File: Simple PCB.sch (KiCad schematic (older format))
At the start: 1 part

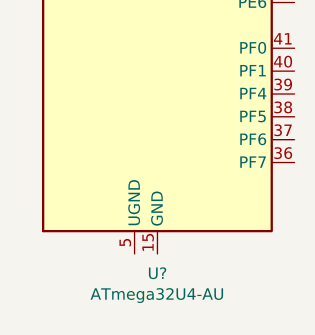
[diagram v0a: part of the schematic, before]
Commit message: Added ground
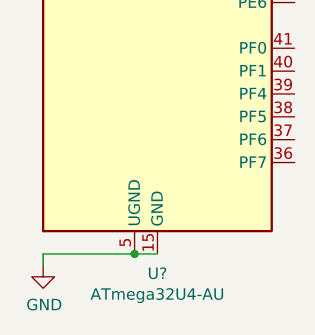
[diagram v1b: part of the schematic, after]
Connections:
- net GND: now reaches U?.15 (GND), U?.23 (GND), U?.35 (GND), U?.43 (GND)
- net GND: now also U?.5 (UGND)
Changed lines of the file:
@@
 EESchema Schematic File Version 4
+LIBS:Simple PCB-cache
 EELAYER 26 0
 EELAYER END
@@
 Wire Wire Line
 	1800 2100 1700 2100
+$Comp
+L power:GND #PWR?
+U 1 1 5C756188
+P 1300 5750
+F 0 "#PWR?" H 1300 5500 50  0001 C CNN
+F 1 "GND" H 1305 5577 50  0000 C CNN
+F 2 "" H 1300 5750 50  0001 C CNN
+F 3 "" H 1300 5750 50  0001 C CNN
+	1    1300 5750
+	1    0    0    -1
+$EndComp
+Wire Wire Line
+	1800 5700 1700 5700
+Wire Wire Line
+	1700 5700 1300 5700
+Wire Wire Line
+	1300 5700 1300 5750
+Connection ~ 1700 5700
 $EndSCHEMATC

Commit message: Finished MCU
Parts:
- added C?: 1uF, symbol Device:C_Small
- added C? (x4): 0.1uF, symbol Device:C_Small
- added C? (x2): 22pF, symbol Device:C_Small
- added R? (x2): 10k, symbol Device:R_Small
- added R? (x2): 22, symbol Device:R_Small
- added SW?: SW_Push, symbol Switch:SW_Push
- added Y?: 16MHz, symbol Device:Crystal_GND24_Small
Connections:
- net +5V: now also U?.7 (VBUS), C?.1, C?.1, C?.1, C?.1, R?.2
- net GND: now also C?.2, C?.2, C?.2, C?.2, C?.2, C?.2, C?.2, R?.1, SW?.1, Y?.2, Y?.4
- net at U?.13 (~RESET): now also R?.1, SW?.2
- net at U?.16 (XTAL2): now also C?.1, Y?.3
- net at U?.17 (XTAL1): now also C?.1, Y?.1
- net at U?.3 (D-): now also R?.1
- net at U?.33 (~HWB~/PE2): now also R?.2
- net at U?.4 (D+): now also R?.1
- net at U?.6 (UCAP): now also C?.1
- new net D+: R?.2
- new net D-: R?.2
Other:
- moved on the sheet: U?

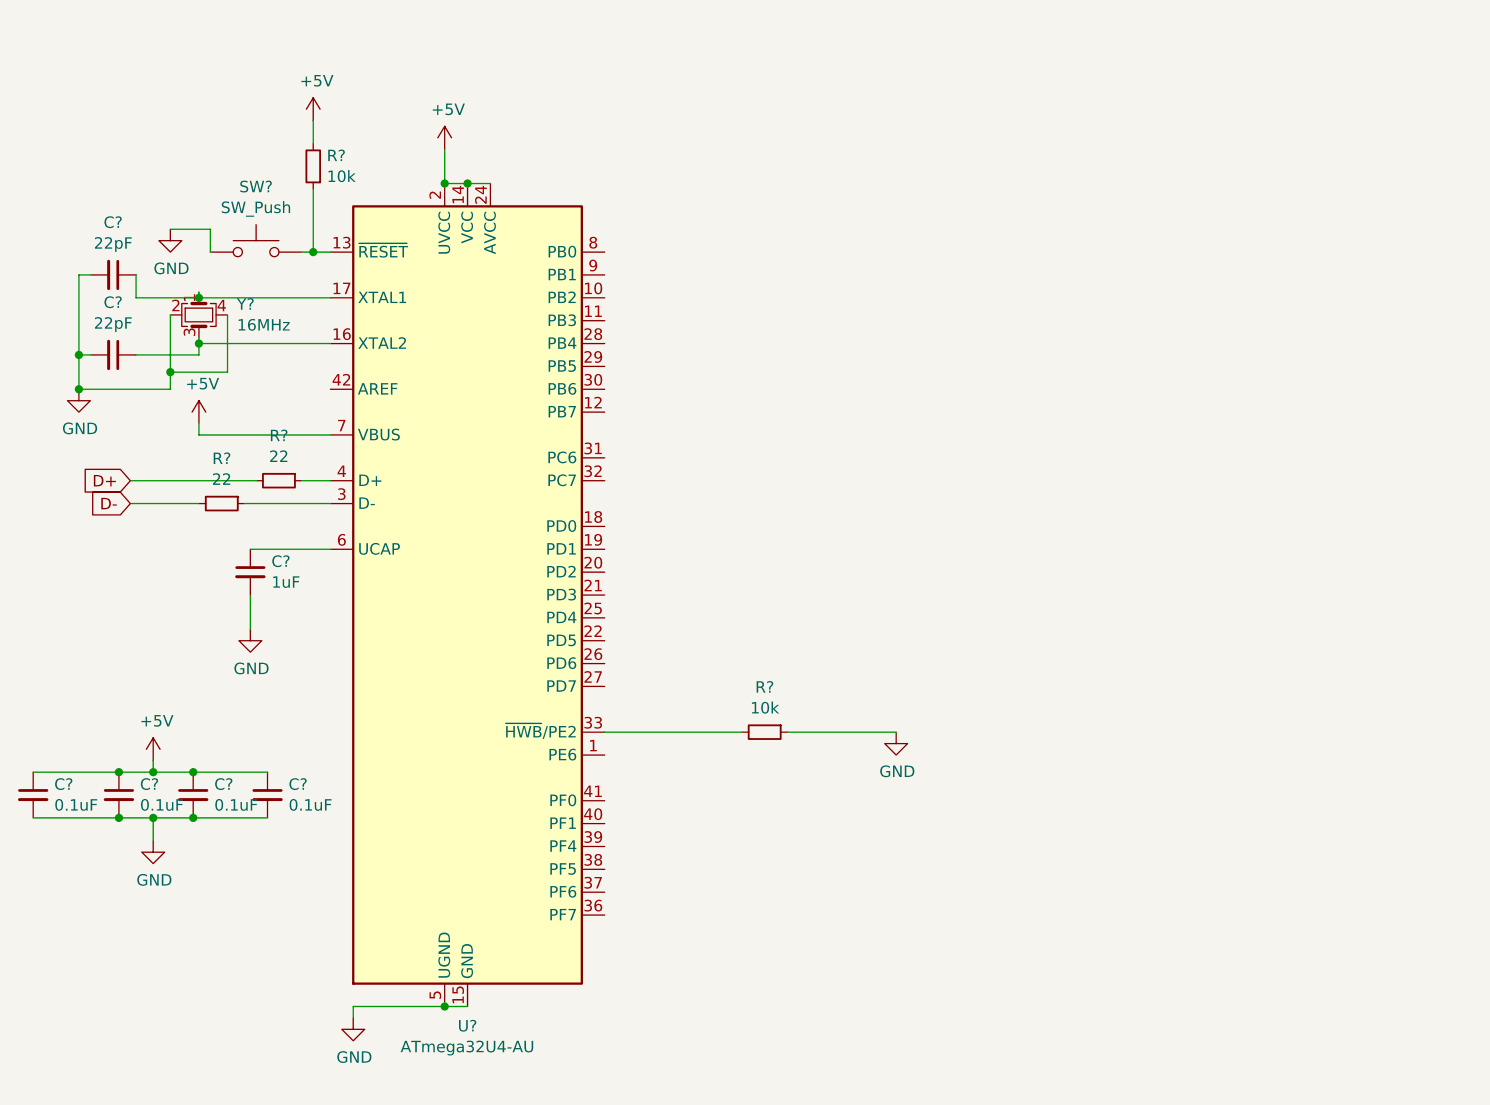
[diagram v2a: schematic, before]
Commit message: Added USB Connector and rows and collums
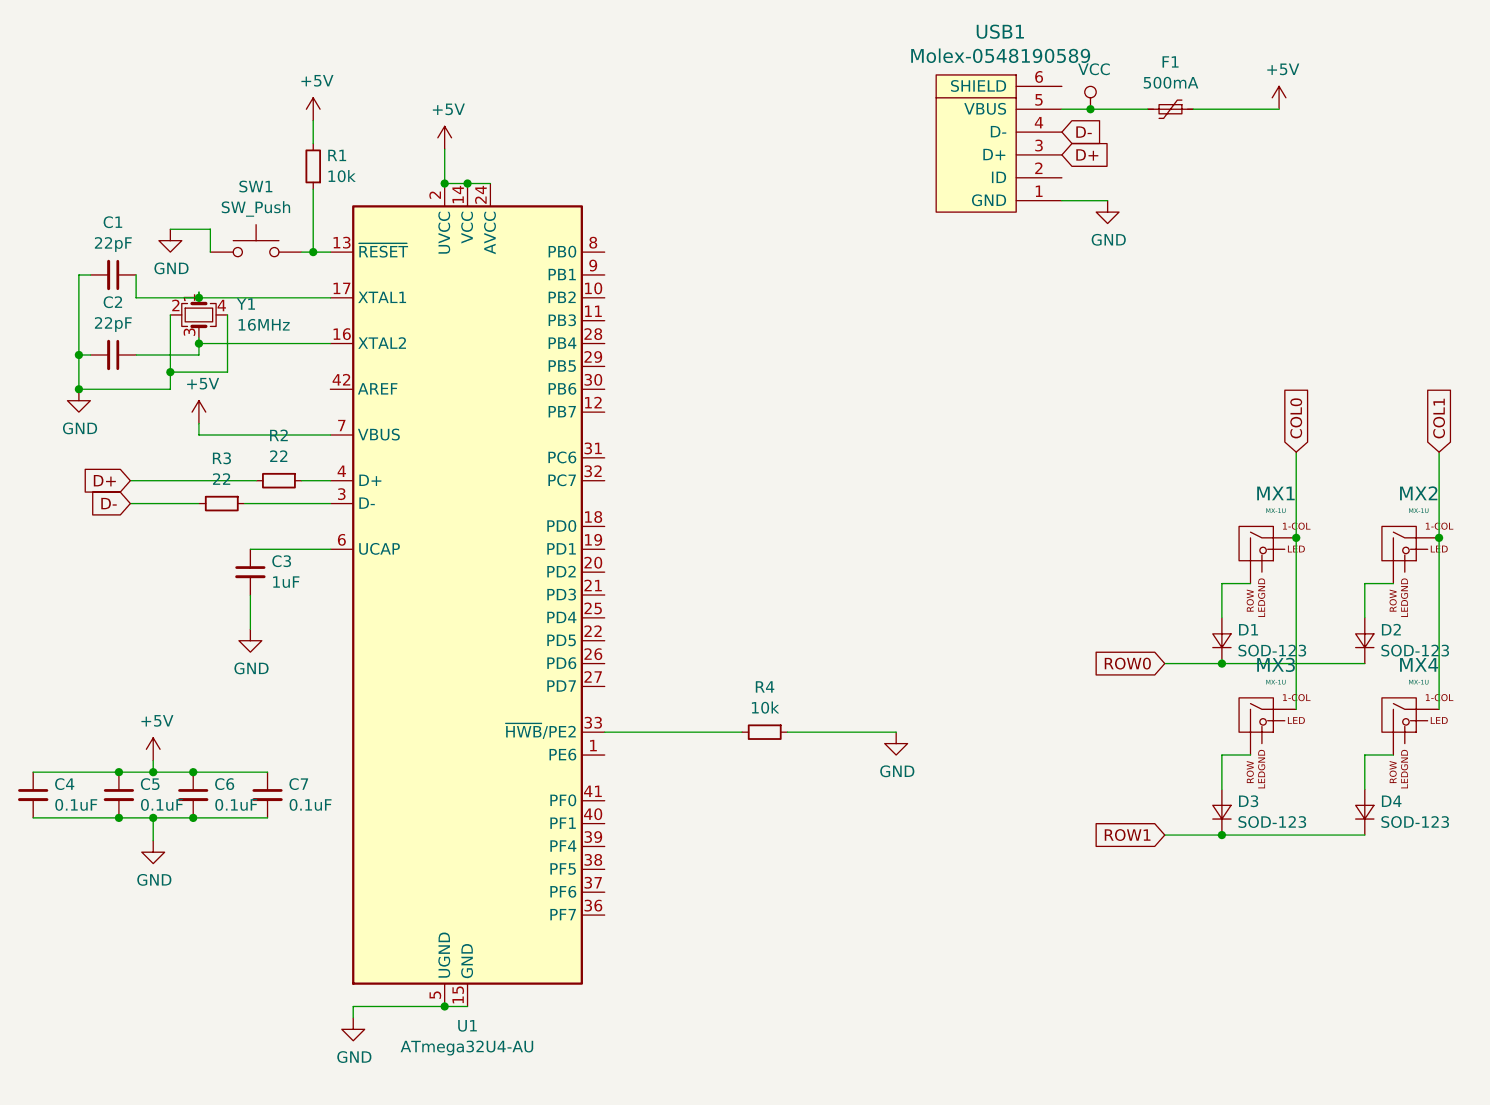
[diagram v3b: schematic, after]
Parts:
- added D1, D2, D3, D4: SOD-123, symbol Device:D_Small
- added F1: 500mA, symbol Device:Polyfuse_Small
- added MX1, MX2, MX3, MX4: MX-1U, symbol MX_Alps_Hybrids:MX-1U
- added USB1: Molex-0548190589, symbol random-keyboard-parts:Molex-0548190589
- gave numbers to parts that had none: 14
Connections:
- net +5V: now also F1.1
- net D+: now also USB1.3 (D+)
- net D-: now also USB1.4 (D-)
- net GND: now also USB1.1 (GND)
- new net: D3.2 (A), MX3.2 (ROW)
- new net: D4.2 (A), MX4.2 (ROW)
- new net: D1.2 (A), MX1.2 (ROW)
- new net: D2.2 (A), MX2.2 (ROW)
- new net COL0: MX1.1 (COL), MX3.1 (COL)
- new net COL1: MX2.1 (COL), MX4.1 (COL)
- new net ROW0: D1.1 (K), D2.1 (K)
- new net ROW1: D3.1 (K), D4.1 (K)
- new net VCC: F1.2, USB1.5 (VBUS)

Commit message: Assigned most footprints
Need to fix 32u4 mcu
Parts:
- C1, C2, C3, C4, C5, C6, C7: footprint (none) -> Capacitor_SMD:C_0805_2012Metric
- D1, D2, D3, D4: footprint (none) -> Diode_SMD:D_SOD-123
- F1: footprint (none) -> Fuse:Fuse_1206_3216Metric
- MX1, MX2, MX3, MX4: footprint (none) -> MX_Alps_Hybrid:MX-1U
- R1, R2, R3, R4: footprint (none) -> Resistor_SMD:R_0805_2012Metric
- SW1: footprint (none) -> random-keyboard-parts:SKQG-1155865
- USB1: footprint (none) -> random-keyboard-parts:Molex-0548190589
- Y1: footprint (none) -> Crystal:Crystal_SMD_3225-4Pin_3.2x2.5mm
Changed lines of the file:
@@
 F 0 "R4" V 4204 4425 50  0000 C CNN
 F 1 "10k" V 4295 4425 50  0000 C CNN
-F 2 "" H 4400 4425 50  0001 C CNN
+F 2 "Resistor_SMD:R_0805_2012Metric" H 4400 4425 50  0001 C CNN
 F 3 "~" H 4400 4425 50  0001 C CNN
 	1    4400 4425
@@
 F 0 "R2" V 2079 3325 50  0000 C CNN
 F 1 "22" V 2170 3325 50  0000 C CNN
-F 2 "" H 2275 3325 50  0001 C CNN
+F 2 "Resistor_SMD:R_0805_2012Metric" H 2275 3325 50  0001 C CNN
 F 3 "~" H 2275 3325 50  0001 C CNN
 	1    2275 3325
@@
 F 0 "R3" V 1829 3425 50  0000 C CNN
 F 1 "22" V 1920 3425 50  0000 C CNN
-F 2 "" H 2025 3425 50  0001 C CNN
+F 2 "Resistor_SMD:R_0805_2012Metric" H 2025 3425 50  0001 C CNN
 F 3 "~" H 2025 3425 50  0001 C CNN
 	1    2025 3425
@@
 F 0 "C3" H 2242 3771 50  0000 L CNN
 F 1 "1uF" H 2242 3680 50  0000 L CNN
-F 2 "" H 2150 3725 50  0001 C CNN
+F 2 "Capacitor_SMD:C_0805_2012Metric" H 2150 3725 50  0001 C CNN
 F 3 "~" H 2150 3725 50  0001 C CNN
 	1    2150 3725
@@
 F 0 "C4" H 1292 4746 50  0000 L CNN
 F 1 "0.1uF" H 1292 4655 50  0000 L CNN
-F 2 "" H 1200 4700 50  0001 C CNN
+F 2 "Capacitor_SMD:C_0805_2012Metric" H 1200 4700 50  0001 C CNN
 F 3 "~" H 1200 4700 50  0001 C CNN
 	1    1200 4700
@@
 F 0 "C5" H 1667 4746 50  0000 L CNN
 F 1 "0.1uF" H 1667 4655 50  0000 L CNN
-F 2 "" H 1575 4700 50  0001 C CNN
+F 2 "Capacitor_SMD:C_0805_2012Metric" H 1575 4700 50  0001 C CNN
 F 3 "~" H 1575 4700 50  0001 C CNN
 	1    1575 4700
@@
 F 0 "C6" H 1992 4746 50  0000 L CNN
 F 1 "0.1uF" H 1992 4655 50  0000 L CNN
-F 2 "" H 1900 4700 50  0001 C CNN
+F 2 "Capacitor_SMD:C_0805_2012Metric" H 1900 4700 50  0001 C CNN
 F 3 "~" H 1900 4700 50  0001 C CNN
 	1    1900 4700
@@
 F 0 "C7" H 2317 4746 50  0000 L CNN
 F 1 "0.1uF" H 2317 4655 50  0000 L CNN
-F 2 "" H 2225 4700 50  0001 C CNN
+F 2 "Capacitor_SMD:C_0805_2012Metric" H 2225 4700 50  0001 C CNN
 F 3 "~" H 2225 4700 50  0001 C CNN
 	1    2225 4700
@@
 F 0 "Y1" V 1879 2766 50  0000 L CNN
 F 1 "16MHz" V 1970 2766 50  0000 L CNN
-F 2 "" H 1925 2600 50  0001 C CNN
+F 2 "Crystal:Crystal_SMD_3225-4Pin_3.2x2.5mm" H 1925 2600 50  0001 C CNN
 F 3 "~" H 1925 2600 50  0001 C CNN
 	1    1925 2600
@@
 F 0 "C1" V 1321 2425 50  0000 C CNN
 F 1 "22pF" V 1412 2425 50  0000 C CNN
-F 2 "" H 1550 2425 50  0001 C CNN
+F 2 "Capacitor_SMD:C_0805_2012Metric" H 1550 2425 50  0001 C CNN
 F 3 "~" H 1550 2425 50  0001 C CNN
 	1    1550 2425
@@
 F 0 "C2" V 1321 2775 50  0000 C CNN
 F 1 "22pF" V 1412 2775 50  0000 C CNN
-F 2 "" H 1550 2775 50  0001 C CNN
+F 2 "Capacitor_SMD:C_0805_2012Metric" H 1550 2775 50  0001 C CNN
 F 3 "~" H 1550 2775 50  0001 C CNN
 	1    1550 2775
@@
 F 0 "SW1" H 2175 2610 50  0000 C CNN
 F 1 "SW_Push" H 2175 2519 50  0000 C CNN
-F 2 "" H 2175 2525 50  0001 C CNN
+F 2 "random-keyboard-parts:SKQG-1155865" H 2175 2525 50  0001 C CNN
 F 3 "" H 2175 2525 50  0001 C CNN
 	1    2175 2325
@@
 F 0 "R1" H 2366 1904 50  0000 R CNN
 F 1 "10k" H 2366 1995 50  0000 R CNN
-F 2 "" H 2425 1950 50  0001 C CNN
+F 2 "Resistor_SMD:R_0805_2012Metric" H 2425 1950 50  0001 C CNN
 F 3 "~" H 2425 1950 50  0001 C CNN
 	1    2425 1950
@@
 F 0 "USB1" V 5937 1869 60  0000 C CNN
 F 1 "Molex-0548190589" V 5831 1869 60  0000 C CNN
-F 2 "" H 5400 1900 60  0001 C CNN
+F 2 "random-keyboard-parts:Molex-0548190589" H 5400 1900 60  0001 C CNN
 F 3 "" H 5400 1900 60  0001 C CNN
 	1    5400 1900
@@
 F 0 "F1" V 5970 1700 50  0000 C CNN
 F 1 "500mA" V 6061 1700 50  0000 C CNN
-F 2 "" H 6225 1500 50  0001 L CNN
+F 2 "Fuse:Fuse_1206_3216Metric" H 6225 1500 50  0001 L CNN
 F 3 "~" H 6175 1700 50  0001 C CNN
 	1    6175 1700
@@
 F 0 "MX3" H 6636 4567 60  0000 C CNN
 F 1 "MX-1U" H 6636 4493 20  0000 C CNN
-F 2 "" H 6525 4325 60  0001 C CNN
+F 2 "MX_Alps_Hybrid:MX-1U" H 6525 4325 60  0001 C CNN
 F 3 "" H 6525 4325 60  0001 C CNN
 	1    6550 4350
@@
 F 0 "D3" V 6446 4707 50  0000 R CNN
 F 1 "SOD-123" V 6355 4707 50  0000 R CNN
-F 2 "" V 6400 4775 50  0001 C CNN
+F 2 "Diode_SMD:D_SOD-123" V 6400 4775 50  0001 C CNN
 F 3 "~" V 6400 4775 50  0001 C CNN
 	1    6400 4775
@@
 F 0 "MX4" H 7261 4567 60  0000 C CNN
 F 1 "MX-1U" H 7261 4493 20  0000 C CNN
-F 2 "" H 7150 4325 60  0001 C CNN
+F 2 "MX_Alps_Hybrid:MX-1U" H 7150 4325 60  0001 C CNN
 F 3 "" H 7150 4325 60  0001 C CNN
 	1    7175 4350
@@
 F 0 "D4" V 7071 4707 50  0000 R CNN
 F 1 "SOD-123" V 6980 4707 50  0000 R CNN
-F 2 "" V 7025 4775 50  0001 C CNN
+F 2 "Diode_SMD:D_SOD-123" V 7025 4775 50  0001 C CNN
 F 3 "~" V 7025 4775 50  0001 C CNN
 	1    7025 4775
@@
 F 0 "MX1" H 6636 3817 60  0000 C CNN
 F 1 "MX-1U" H 6636 3743 20  0000 C CNN
-F 2 "" H 6525 3575 60  0001 C CNN
+F 2 "MX_Alps_Hybrid:MX-1U" H 6525 3575 60  0001 C CNN
 F 3 "" H 6525 3575 60  0001 C CNN
 	1    6550 3600
@@
 F 0 "D1" V 6446 3957 50  0000 R CNN
 F 1 "SOD-123" V 6355 3957 50  0000 R CNN
-F 2 "" V 6400 4025 50  0001 C CNN
+F 2 "Diode_SMD:D_SOD-123" V 6400 4025 50  0001 C CNN
 F 3 "~" V 6400 4025 50  0001 C CNN
 	1    6400 4025
@@
 F 0 "MX2" H 7261 3817 60  0000 C CNN
 F 1 "MX-1U" H 7261 3743 20  0000 C CNN
-F 2 "" H 7150 3575 60  0001 C CNN
+F 2 "MX_Alps_Hybrid:MX-1U" H 7150 3575 60  0001 C CNN
 F 3 "" H 7150 3575 60  0001 C CNN
 	1    7175 3600
@@
 F 0 "D2" V 7071 3957 50  0000 R CNN
 F 1 "SOD-123" V 6980 3957 50  0000 R CNN
-F 2 "" V 7025 4025 50  0001 C CNN
+F 2 "Diode_SMD:D_SOD-123" V 7025 4025 50  0001 C CNN
 F 3 "~" V 7025 4025 50  0001 C CNN
 	1    7025 4025
